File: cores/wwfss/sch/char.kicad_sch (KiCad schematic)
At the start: 23 parts, among them IC10 74LS157, IC11 74LS157, IC14 74LS04, IC18 74LS32, IC22 RAM_2016, IC25 74LS10, IC26 74LS74, IC3 74LS04, IC31 74LS174, IC32 74LS245, IC36 74LS30, IC37 74LS00, IC40 74LS273, IC41 74LS174, IC42 74LS273, IC43 74LS273, IC64 74LS04, IC68 74LS00, IC69 74LS10, IC72 74LS04, IC82 74LS74, IC9 74LS157, IC94 74LS32

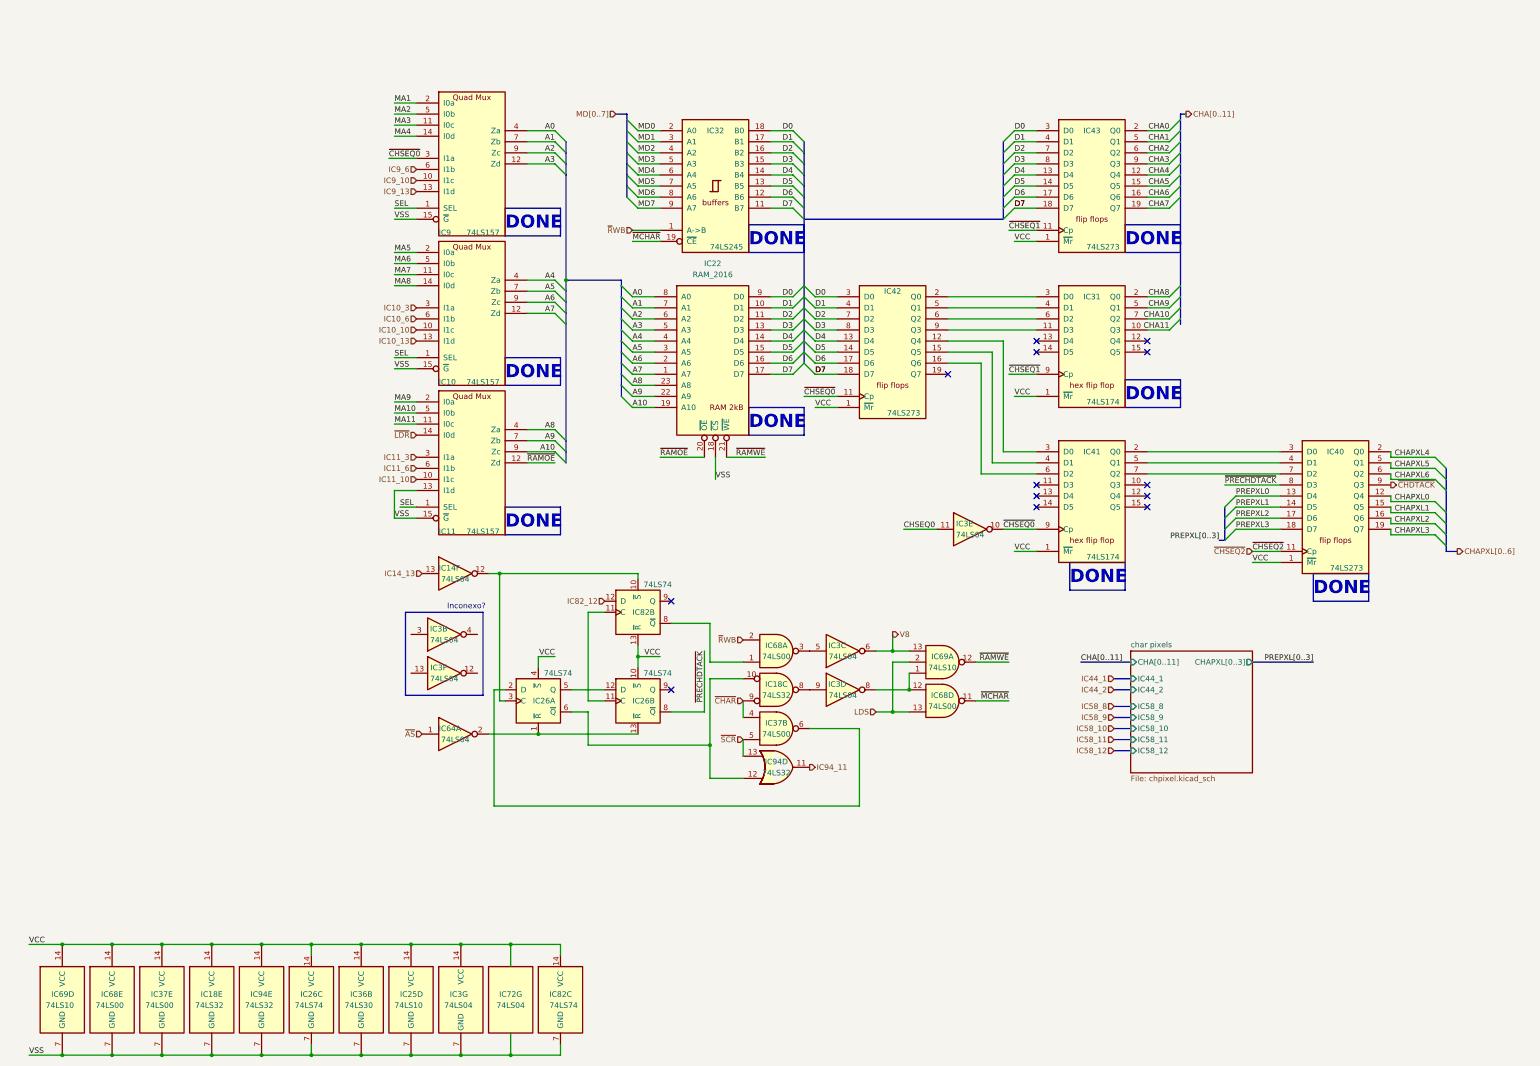
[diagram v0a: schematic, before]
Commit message: wwfss: new core compatible with WWF Super Stars enters beta phase dd: correct polarity for VBL signal in main
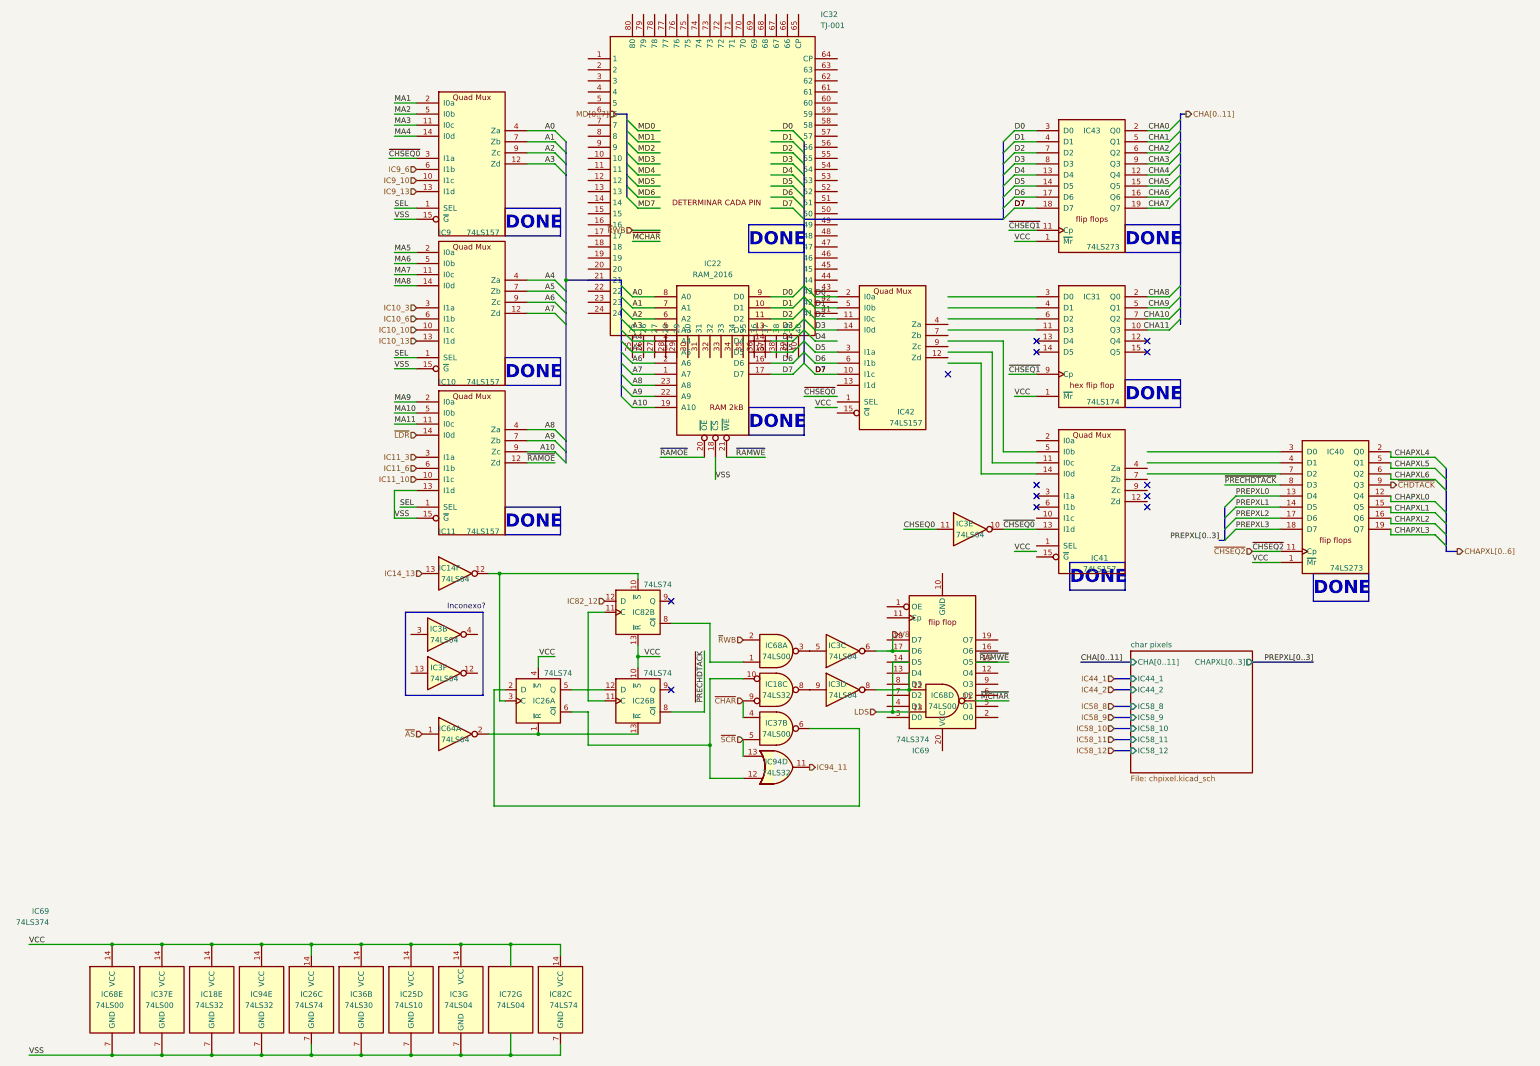
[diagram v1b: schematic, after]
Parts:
- IC32: value 74LS245 -> TJ-001
- IC41: value 74LS174 -> 74LS157
- IC42: value 74LS273 -> 74LS157
- IC69: value 74LS10 -> 74LS374
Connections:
- net D0: now also IC42.2 (I0a); no longer IC32.18 (B0), IC42.3 (D0)
- net D1: now also IC42.5 (I0b); no longer IC32.17 (B1), IC42.4 (D1)
- net D2: now also IC42.11 (I0c); no longer IC32.16 (B2), IC42.7 (D2)
- net D3: now also IC42.14 (I0d); no longer IC32.15 (B3), IC42.8 (D3)
- net D4: no longer IC32.14 (B4), IC42.13 (D4)
- net D5: now also IC42.3 (I1a); no longer IC32.13 (B5), IC42.14 (D5)
- net D6: now also IC42.6 (I1b); no longer IC32.12 (B6), IC42.17 (D6)
- net D7: now also IC42.10 (I1c); no longer IC32.11 (B7), IC42.18 (D7)
- net LDS: no longer IC69.2
- net MD0: no longer IC32.2 (A0)
- net MD1: no longer IC32.3 (A1)
- net MD2: no longer IC32.4 (A2)
- net MD3: no longer IC32.5 (A3)
- net MD4: no longer IC32.6 (A4)
- net MD5: no longer IC32.7 (A5)
- net MD6: no longer IC32.8 (A6)
- net MD7: no longer IC32.9 (A7)
- net V8: no longer IC69.13
- net VCC: no longer IC41.1 (~{Mr}), IC41.16 (VCC), IC42.1 (~{Mr}), IC69.14 (VCC)
- net VSS: no longer IC41.8 (VSS), IC69.7 (GND)
- net ~{CHSEQ0}: now also IC41.13 (I1d); no longer IC41.9 (Cp), IC42.11 (Cp)
- net ~{MCHAR}: no longer IC32.19 (~{CE})
- net ~{RAMWE}: no longer IC69.12
- net ~{R}WB: no longer IC32.1 (A->B)
- net at IC41.2 (I0a): no longer IC40.3 (D0)
- net at IC41.3 (I1a): no longer IC42.12 (Q4)
- net at IC41.4 (Za): no longer IC42.15 (Q5)
- net at IC41.5 (I0b): no longer IC40.4 (D1)
- net at IC41.6 (I1b): no longer IC42.16 (Q6)
- net at IC41.7 (Zb): no longer IC40.7 (D2)
- net at IC31.11 (D3): no longer IC42.9 (Q3)
- net at IC31.3 (D0): no longer IC42.2 (Q0)
- net at IC31.4 (D1): no longer IC42.5 (Q1)
- net at IC31.6 (D2): no longer IC42.6 (Q2)
- net at IC3.8, IC68.12: no longer IC69.1
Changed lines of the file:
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@@
 	)
 	(junction
-		(at 21.59 283.21)
-		(diameter 0)
-		(color 0 0 0 0)
-	)
-	(junction
 		(at 78.74 283.21)
 		(diameter 0)
@@
 	)
 	(junction
-		(at 21.59 257.81)
-		(diameter 0)
-		(color 0 0 0 0)
-	)
-	(junction
 		(at 124.46 257.81)
 		(diameter 0)
@@
 	(wire
 		(pts
-			(xy 13.97 257.81) (xy 21.59 257.81)
+			(xy 13.97 257.81) (xy 33.02 257.81)
 		)
 		(stroke
@@
 	(wire
 		(pts
-			(xy 13.97 283.21) (xy 21.59 283.21)
+			(xy 13.97 283.21) (xy 33.02 283.21)
 		)
 		(stroke
@@
 	(wire
 		(pts
-			(xy 21.59 257.81) (xy 33.02 257.81)
-		)
-		(stroke
-			(width 0)
-			(type default)
-		)
-	)
-	(wire
-		(pts
 			(xy 153.67 73.66) (xy 158.75 73.66)
 		)
@@
 		)
 	)
-	(wire
-		(pts
-			(xy 21.59 283.21) (xy 33.02 283.21)
-		)
-		(stroke
-			(width 0)
-			(type default)
-		)
-	)
 	(bus
 		(pts
@@
 	)
 	(symbol
+		(lib_name "74LS174_1")
 		(lib_id "jt74:74LS174")
 		(at 257.81 154.94 0)
@@
 		(dnp no)
 		(property "Reference" "IC41"
-			(at 257.81 144.78 0)
+			(at 259.588 169.164 0)
 			(effects
 				(font
@@
 			)
 		)
-		(property "Value" "74LS174"
-			(at 260.35 168.91 0)
+		(property "Value" "74LS157"
+			(at 259.588 171.704 0)
 			(effects
 				(font
@@
 			)
 		)
-		(property "Datasheet" "http://www.ti.com/lit/gpn/sn74LS174"
-			(at 259.08 173.99 0)
+		(property "Datasheet" "https://www.alldatasheet.com/datasheet-pdf/pdf/27402/TI/74LS157.html"
+			(at 257.81 173.99 0)
 			(effects
 				(font
@@
 			)
 		)
-		(property "Description" "Hex D-type Flip-Flop, reset"
+		(property "Description" "Quad 2 to 1 line Multiplexer"
 			(at 257.81 154.94 0)
 			(effects
@@
 		(pin "9"
 		)
-		(pin "16"
-		)
-		(pin "8"
-		)
 		(instances
 			(project "wwfsstar"
@@
 		(dnp no)
 		(property "Reference" "IC32"
-			(at 171.45 71.12 0)
+			(at 195.58 44.45 0)
 			(effects
 				(font
 					(size 1.27 1.27)
 				)
+				(justify left)
 			)
 		)
-		(property "Value" "74LS245"
-			(at 173.99 97.79 0)
+		(property "Value" "TJ-001"
+			(at 195.58 46.99 0)
 			(effects
 				(font
 					(size 1.27 1.27)
 				)
+				(justify left)
 			)
 		)
 		(property "Footprint" ""
-			(at 171.45 83.82 0)
+			(at 148.59 99.06 0)
 			(effects
 				(font
@@
 			)
 		)
-		(property "Datasheet" "http://www.ti.com/lit/gpn/sn74LS245"
-			(at 171.45 83.82 0)
+		(property "Datasheet" ""
+			(at 148.59 99.06 0)
 			(effects
 				(font
@@
 			)
 		)
-		(property "Description" "Octal BUS Transceivers, 3-State outputs"
-			(at 171.45 83.82 0)
+		(property "Description" ""
+			(at 148.59 99.06 0)
 			(effects
 				(font
@@
 		(pin "9"
 		)
+		(pin "22"
+		)
+		(pin "31"
+		)
+		(pin "63"
+		)
+		(pin "62"
+		)
+		(pin "35"
+		)
+		(pin "27"
+		)
+		(pin "39"
+		)
+		(pin "37"
+		)
+		(pin "36"
+		)
+		(pin "32"
+		)
+		(pin "29"
+		)
+		(pin "38"
+		)
+		(pin "69"
+		)
+		(pin "47"
+		)
+		(pin "60"
+		)
+		(pin "78"
+		)
+		(pin "67"
+		)
+		(pin "25"
+		)
+		(pin "61"
+		)
+		(pin "30"
+		)
+		(pin "34"
+		)
+		(pin "80"
+		)
+		(pin "43"
+		)
+		(pin "55"
+		)
+		(pin "53"
+		)
+		(pin "79"
+		)
+		(pin "49"
+		)
+		(pin "50"
+		)
+		(pin "75"
+		)
+		(pin "24"
+		)
+		(pin "45"
+		)
+		(pin "26"
+		)
+		(pin "58"
+		)
+		(pin "23"
+		)
+		(pin "52"
+		)
+		(pin "51"
+		)
+		(pin "77"
+		)
+		(pin "59"
+		)
+		(pin "40"
+		)
+		(pin "65"
+		)
+		(pin "33"
+		)
+		(pin "28"
+		)
+		(pin "54"
+		)
+		(pin "57"
+		)
+		(pin "66"
+		)
+		(pin "56"
+		)
+		(pin "64"
+		)
+		(pin "76"
+		)
+		(pin "70"
+		)
+		(pin "46"
+		)
+		(pin "72"
+		)
+		(pin "74"
+		)
+		(pin "21"
+		)
+		(pin "42"
+		)
+		(pin "10"
+		)
+		(pin "20"
+		)
+		(pin "71"
+		)
+		(pin "68"
+		)
+		(pin "73"
+		)
+		(pin "44"
+		)
+		(pin "41"
+		)
+		(pin "48"
+		)
 		(instances
-			(project "wwfsstar"
+			(project ""
+				(path "/9b45fe8f-ccde-4083-bbaa-82d9a9454022/004a228e-24de-4680-a954-fe1a8a16228f/e6a3df50-9bb2-4bc8-8ffc-08ab5893909a"
+					(reference "IC32")
+					(unit 1)
+				)
 				(path "/9b45fe8f-ccde-4083-bbaa-82d9a9454022/196e9cfe-efe3-4c2b-8678-7a6099cf4b06/e23a4357-b221-46f5-8d95-f07964f6206a"
 					(reference "IC32")
@@
 	)
 	(symbol
+		(lib_name "74LS10_2")
 		(lib_id "74xx:74LS10")
 		(at 21.59 270.51 0)
@@
 		(dnp no)
 		(property "Reference" "IC69"
-			(at 19.05 269.24 0)
+			(at 18.5735 250.19 0)
 			(effects
 				(font
 					(size 1.27 1.27)
 				)
-				(justify left)
+				(justify right)
 			)
 		)
-		(property "Value" "74LS10"
-			(at 17.78 271.78 0)
+		(property "Value" "74LS374"
+			(at 18.5735 252.73 0)
 			(effects
 				(font
 					(size 1.27 1.27)
 				)
-				(justify left)
+				(justify right)
 			)
 		)
@@
 			)
 		)
-		(property "Datasheet" "http://www.ti.com/lit/gpn/sn74LS10"
+		(property "Datasheet" "http://www.ti.com/lit/gpn/sn74LS374"
 			(at 21.59 270.51 0)
 			(effects
@@
 			)
 		)
-		(property "Description" "Triple 3-input NAND"
+		(property "Description" "8-bit Register, 3-state outputs"
 			(at 21.59 270.51 0)
 			(effects
@@
 		(pin "7"
 		)
+		(pin "15"
+		)
+		(pin "16"
+		)
+		(pin "17"
+		)
+		(pin "18"
+		)
+		(pin "19"
+		)
+		(pin "20"
+		)
 		(instances
 			(project "wwfsstar"
@@
 	)
 	(symbol
+		(lib_name "74LS10_1")
 		(lib_id "74xx:74LS10")
 		(at 223.52 193.04 0)
@@
 		(dnp no)
 		(property "Reference" "IC69"
-			(at 223.52 191.77 0)
+			(at 220.5035 213.36 0)
 			(effects
 				(font
 					(size 1.27 1.27)
 				)
+				(justify right)
 			)
 		)
-		(property "Value" "74LS10"
-			(at 223.52 194.31 0)
+		(property "Value" "74LS374"
+			(at 220.5035 210.82 0)
 			(effects
 				(font
 					(size 1.27 1.27)
 				)
+				(justify right)
 			)
 		)
@@
 			)
 		)
-		(property "Datasheet" "http://www.ti.com/lit/gpn/sn74LS10"
+		(property "Datasheet" "http://www.ti.com/lit/gpn/sn74LS374"
 			(at 223.52 193.04 0)
 			(effects
@@
 			)
 		)
-		(property "Description" "Triple 3-input NAND"
+		(property "Description" "8-bit Register, 3-state outputs"
 			(at 223.52 193.04 0)
 			(effects
@@
 		(pin "7"
 		)
+		(pin "19"
+		)
+		(pin "17"
+		)
+		(pin "18"
+		)
+		(pin "15"
+		)
+		(pin "16"
+		)
+		(pin "20"
+		)
 		(instances
 			(project "wwfsstar"
@@
 	)
 	(symbol
+		(lib_name "74LS273_1")
 		(lib_id "jt74:74LS273")
 		(at 212.09 121.92 0)
@@
 		(dnp no)
 		(property "Reference" "IC42"
-			(at 212.09 107.95 0)
+			(at 215.138 135.636 0)
 			(effects
 				(font
@@
 			)
 		)
-		(property "Value" "74LS273"
-			(at 214.63 135.89 0)
+		(property "Value" "74LS157"
+			(at 215.138 138.176 0)
 			(effects
 				(font
@@
 			)
 		)
-		(property "Datasheet" "http://www.ti.com/lit/gpn/sn74LS273"
-			(at 212.09 121.92 0)
+		(property "Datasheet" "https://www.alldatasheet.com/datasheet-pdf/pdf/27402/TI/74LS157.html"
+			(at 212.09 140.97 0)
 			(effects
 				(font
@@
 			)
 		)
-		(property "Description" "8-bit D Flip-Flop, reset"
+		(property "Description" "Quad 2 to 1 line Multiplexer"
 			(at 212.09 121.92 0)
 			(effects
@@
 		(pin "15"
 		)
-		(pin "16"
-		)
-		(pin "17"
-		)
-		(pin "18"
-		)
-		(pin "19"
+		(pin "10"
 		)
 		(pin "2"
@@
 		(pin "7"
 		)
-		(pin "8"
-		)
 		(pin "9"

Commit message: wwfss sch
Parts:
- IC3: value 74LS04 -> 74LS10
- IC32: value TJ-001 -> 74LS245
- IC41: value 74LS157 -> 74LS174
- IC42: value 74LS157 -> 74LS273
- IC69: value 74LS374 -> 74LS10
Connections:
- net CHSEQ0: no longer IC3.11
- net D0: now also IC32.18 (B0), IC42.3 (D0); no longer IC42.2 (I0a)
- net D1: now also IC32.17 (B1), IC42.4 (D1); no longer IC42.5 (I0b)
- net D2: now also IC32.16 (B2), IC42.7 (D2); no longer IC42.11 (I0c)
- net D3: now also IC32.15 (B3), IC42.8 (D3); no longer IC42.14 (I0d)
- net D4: now also IC32.14 (B4), IC42.13 (D4)
- net D5: now also IC32.13 (B5), IC42.14 (D5); no longer IC42.3 (I1a)
- net D6: now also IC32.12 (B6), IC42.17 (D6); no longer IC42.6 (I1b)
- net D7: now also IC32.11 (B7), IC42.18 (D7); no longer IC42.10 (I1c)
- net LDS: now also IC69.2
- net MD0: now also IC32.2 (A0)
- net MD1: now also IC32.3 (A1)
- net MD2: now also IC32.4 (A2)
- net MD3: now also IC32.5 (A3)
- net MD4: now also IC32.6 (A4)
- net MD5: now also IC32.7 (A5)
- net MD6: now also IC32.8 (A6)
- net MD7: now also IC32.9 (A7)
- net V8: now also IC3.8, IC69.13; no longer IC3.6
- net VCC: now also IC3.14 (VCC), IC41.1 (~{Mr}), IC41.16 (VCC), IC42.1 (~{Mr}), IC69.14 (VCC); no longer IC3.14 (VCC)
- net VSS: now also IC41.8 (VSS), IC69.7 (GND); no longer IC3.7 (GND)
- net ~{CHSEQ0}: now also IC41.9 (Cp), IC42.11 (Cp); no longer IC3.10, IC41.13 (I1d)
- net ~{MCHAR}: now also IC32.19 (~{CE})
- net ~{RAMWE}: now also IC69.12
- net ~{R}WB: now also IC32.1 (A->B)
- net at IC18.8: no longer IC3.9
- net at IC41.2 (Q0): now also IC40.3 (D0)
- net at IC41.3 (D0): now also IC42.12 (Q4)
- net at IC41.4 (D1): now also IC42.15 (Q5)
- net at IC41.5 (Q1): now also IC40.4 (D1)
- net at IC41.6 (D2): now also IC42.16 (Q6)
- net at IC41.7 (Q2): now also IC40.7 (D2)
- net at IC31.11 (D3): now also IC42.9 (Q3)
- net at IC31.3 (D0): now also IC42.2 (Q0)
- net at IC31.4 (D1): now also IC42.5 (Q1)
- net at IC31.6 (D2): now also IC42.6 (Q2)
- net at IC69.1: now also IC68.12
- net at IC68.3: now also IC3.10; no longer IC3.5
- new net GND: IC3.7 (GND)

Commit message: schematic work
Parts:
- removed unit 5 of IC3
- added IC95: 74LS10, symbol 74xx:74LS04
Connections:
- net VSS is gone; now on net GND: IC10.15 (~{G}), IC11.13 (I1d), IC11.15 (~{G}), IC18.7 (GND), IC22.18 (~{CS}), IC25.7 (GND), IC26.7 (GND), IC31.8 (VSS), IC36.7 (GND), IC37.7 (GND), IC41.8 (VSS), IC68.7 (GND), IC69.7 (GND), IC72.7 (VSS), IC82.7 (GND), IC9.15 (~{G}), IC94.7 (GND)
- net GND: now also IC95.7 (GND)
- net MA1: now also IC18.8
- net VCC: now also IC95.14 (VCC)
- net IC14_11: now reaches IC26.11 (C), IC82.11 (C)
- no-connect marks 13 -> 17
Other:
- note removed: "DONE"
- note removed: "Inconexo?"
- moved on the sheet: IC3D
